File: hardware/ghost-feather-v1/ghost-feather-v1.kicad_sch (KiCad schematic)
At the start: 71 parts, among them J1 Conn_ARM_SWD_TagConnect_TC2030, J2 USB_C_Receptacle_USB2.0, J3 Conn_01x03, J4 Conn_01x03, J5 Conn_01x03, J6 Conn_01x03, J7 Conn_01x08, Q1 BSS138, Q2 BSS138, Q3 BSS138, Q4 BSS138, SW2 BOOT0, U1 STM32F722RETx, U2 BMI270, U3 USBLC6-2SC6_MOD, U4 MPM3610, U5 MPM3610, X1 16MHz, X2 32kHz768

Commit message: feat: Add crystal and clock oscillator footprints #1
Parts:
- C1: footprint Capacitor_SMD:C_0603_1608Metric -> ghost-feather-v1:CC4V-T1A-32.768kHz
- X1: footprint (none) -> ghost-feather-v1:AMPMGFB_1.6mm1.2mm_16MHz
- X2: footprint (none) -> ghost-feather-v1:CC4V-T1A-32.768kHz
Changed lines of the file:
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@@
       (effects (font (size 1.27 1.27)))
     )
-    (property "Footprint" "" (at 328.93 116.84 0)
+    (property "Footprint" "ghost-feather-v1:AMPMGFB_1.6mm1.2mm_16MHz" (at 328.93 116.84 0)
       (effects (font (size 1.27 1.27)) hide)
     )
@@
       (effects (font (size 1.27 1.27)) (justify right))
     )
-    (property "Footprint" "" (at 317.5 165.1 0)
+    (property "Footprint" "ghost-feather-v1:CC4V-T1A-32.768kHz" (at 317.5 165.1 0)
       (effects (font (size 1.27 1.27)) hide)
     )
@@
       (effects (font (size 1.27 1.27)) (justify right))
     )
-    (property "Footprint" "Capacitor_SMD:C_0603_1608Metric" (at 247.65 92.71 0)
-      (effects (font (size 1.27 1.27)) hide)
-    )
+    (property "Footprint" "ghost-feather-v1:CC4V-T1A-32.768kHz" (at 247.65 92.71 0)
+      (effects (font (size 1.27 1.27)) hide)
+    )

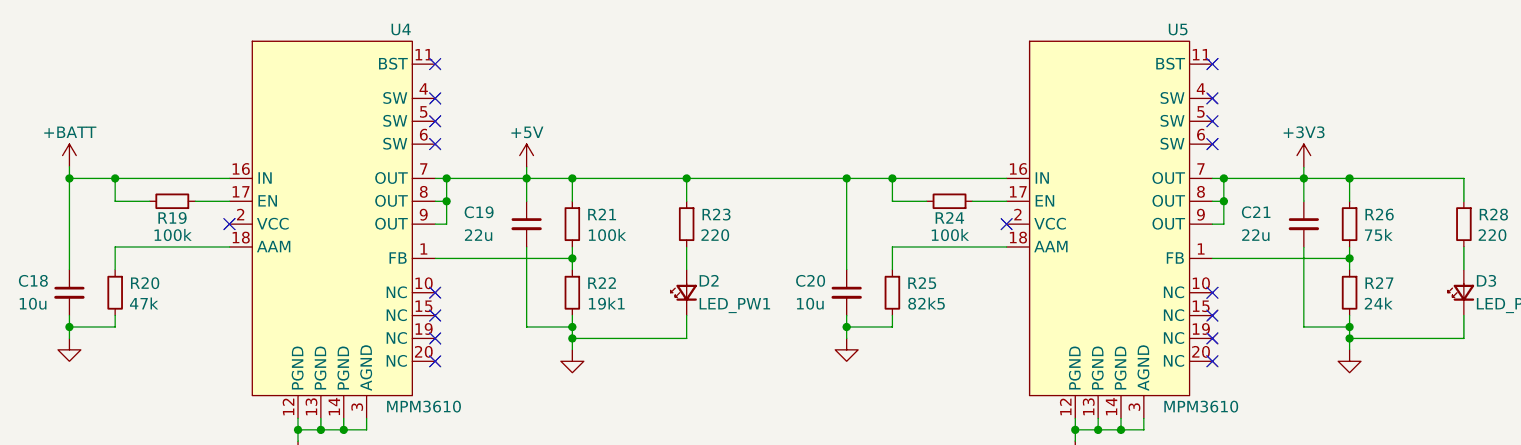
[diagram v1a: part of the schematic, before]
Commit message: feat: Add power flags to pass ERC
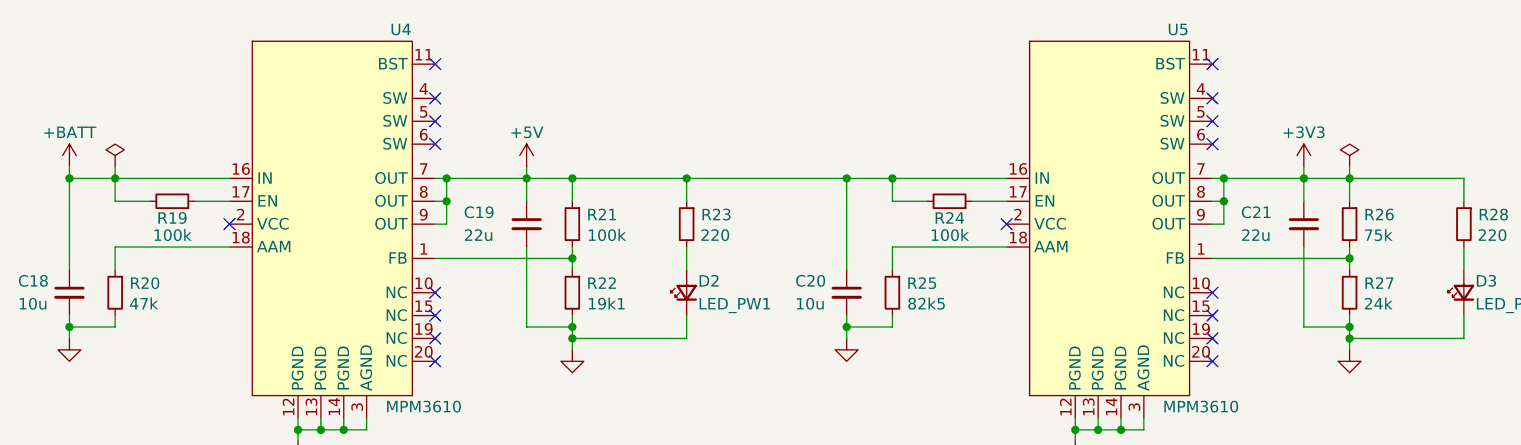
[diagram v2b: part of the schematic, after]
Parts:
- C1: footprint ghost-feather-v1:CC4V-T1A-32.768kHz -> Capacitor_SMD:C_0402_1005Metric
- SW2: footprint Connector_USB:USB_C_Receptacle_GCT_USB4085 -> Button_Switch_SMD:SW_SPST_EVQPE1
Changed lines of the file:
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@@
     (stroke (width 0) (type default))
   )
+  (wire (pts (xy 80.01 46.99) (xy 80.01 48.26))
+    (stroke (width 0) (type default))
+  )
   (wire (pts (xy 167.64 189.23) (xy 168.91 189.23))
     (stroke (width 0) (type default))
@@
     (stroke (width 0) (type default))
   )
+  (wire (pts (xy 217.17 46.99) (xy 217.17 48.26))
+    (stroke (width 0) (type default))
+  )
   (wire (pts (xy 116.84 53.34) (xy 116.84 50.8))
     (stroke (width 0) (type default))
@@
     )
   )
+  (symbol (lib_id "power:PWR_FLAG") (at 217.17 46.99 0) (unit 1)
+    (in_bom yes) (on_board yes) (dnp no) (fields_autoplaced)
+    (property "Reference" "#FLG04" (at 217.17 45.085 0)
+      (effects (font (size 1.27 1.27)) hide)
+    )
+    (property "Value" "PWR_FLAG" (at 217.17 41.91 0)
+      (effects (font (size 1.27 1.27)) hide)
+    )
+    (property "Footprint" "" (at 217.17 46.99 0)
+      (effects (font (size 1.27 1.27)) hide)
+    )
+    (property "Datasheet" "~" (at 217.17 46.99 0)
+      (effects (font (size 1.27 1.27)) hide)
+    )
+    (pin "1")
+    (instances
+      (project "ghost-feather-v1"
+        (path "/e4b634d1-7d64-4f26-a94e-3707be1de22a"
+          (reference "#FLG04") (unit 1)
+        )
+      )
+    )
+  )
   (symbol (lib_id "Device:C_Small") (at 298.45 92.71 0) (mirror y) (unit 1)
     (in_bom yes) (on_board yes) (dnp no) (fields_autoplaced)
@@
     )
   )
+  (symbol (lib_id "power:PWR_FLAG") (at 80.01 46.99 0) (unit 1)
+    (in_bom yes) (on_board yes) (dnp no) (fields_autoplaced)
+    (property "Reference" "#FLG03" (at 80.01 45.085 0)
+      (effects (font (size 1.27 1.27)) hide)
+    )
+    (property "Value" "PWR_FLAG" (at 80.01 41.91 0)
+      (effects (font (size 1.27 1.27)) hide)
+    )
+    (property "Footprint" "" (at 80.01 46.99 0)
+      (effects (font (size 1.27 1.27)) hide)
+    )
+    (property "Datasheet" "~" (at 80.01 46.99 0)
+      (effects (font (size 1.27 1.27)) hide)
+    )
+    (pin "1")
+    (instances
+      (project "ghost-feather-v1"
+        (path "/e4b634d1-7d64-4f26-a94e-3707be1de22a"
+          (reference "#FLG03") (unit 1)
+        )
+      )
+    )
+  )
   (symbol (lib_id "power:GND") (at 308.61 107.95 0) (mirror y) (unit 1)
     (in_bom yes) (on_board yes) (dnp no) (fields_autoplaced)
@@
       (effects (font (size 1.27 1.27)))
     )
-    (property "Footprint" "Connector_USB:USB_C_Receptacle_GCT_USB4085" (at 344.17 130.81 0)
+    (property "Footprint" "Button_Switch_SMD:SW_SPST_EVQPE1" (at 344.17 130.81 0)
       (effects (font (size 1.27 1.27)) hide)
     )
@@
       (effects (font (size 1.27 1.27)) (justify right))
     )
-    (property "Footprint" "ghost-feather-v1:CC4V-T1A-32.768kHz" (at 247.65 92.71 0)
+    (property "Footprint" "Capacitor_SMD:C_0402_1005Metric" (at 247.65 92.71 0)
       (effects (font (size 1.27 1.27)) hide)
     )

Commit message: feat: Components placement on PCB #2
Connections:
- net RF_CH0: now also U1.35 (PB14); no longer U1.37 (PC6)
- net RF_CH1: now also U1.36 (PB15); no longer U1.38 (PC7)
- net RF_CH2: now also U1.37 (PC6); no longer U1.39 (PC8)
- net RF_CH3: now also U1.38 (PC7); no longer U1.40 (PC9)
- net RF_CH4: now also U1.39 (PC8); no longer U1.36 (PB15)
- net RF_CH5: now also U1.40 (PC9); no longer U1.35 (PB14)
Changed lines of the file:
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@@
+    (stroke (width 0) (type default))
+  )
+  (wire (pts (xy 353.06 153.67) (xy 335.28 153.67))
     (stroke (width 0) (type default))
   )
@@
     (stroke (width 0) (type default))
   )
-  (wire (pts (xy 290.83 146.05) (xy 353.06 146.05))
-    (stroke (width 0) (type default))
-  )
   (wire (pts (xy 189.23 76.2) (xy 189.23 74.93))
     (stroke (width 0) (type default))
@@
     (stroke (width 0) (type default))
   )
+  (wire (pts (xy 347.98 143.51) (xy 347.98 207.01))
+    (stroke (width 0) (type default))
+  )
   (wire (pts (xy 237.49 148.59) (xy 227.33 148.59))
     (stroke (width 0) (type default))
@@
     (stroke (width 0) (type default))
   )
-  (wire (pts (xy 290.83 151.13) (xy 353.06 151.13))
-    (stroke (width 0) (type default))
-  )
   (wire (pts (xy 303.53 168.91) (xy 303.53 166.37))
     (stroke (width 0) (type default))
@@
     (stroke (width 0) (type default))
   )
+  (wire (pts (xy 353.06 148.59) (xy 340.36 148.59))
+    (stroke (width 0) (type default))
+  )
   (wire (pts (xy 217.17 219.71) (xy 217.17 217.17))
     (stroke (width 0) (type default))
@@
     (stroke (width 0) (type default))
   )
+  (wire (pts (xy 345.44 146.05) (xy 353.06 146.05))
+    (stroke (width 0) (type default))
+  )
   (wire (pts (xy 336.55 130.81) (xy 339.09 130.81))
     (stroke (width 0) (type default))
@@
     (stroke (width 0) (type default))
   )
+  (wire (pts (xy 340.36 148.59) (xy 340.36 143.51))
+    (stroke (width 0) (type default))
+  )
   (wire (pts (xy 208.28 247.65) (xy 217.17 247.65))
     (stroke (width 0) (type default))
@@
     (stroke (width 0) (type default))
   )
-  (wire (pts (xy 243.84 207.01) (xy 345.44 207.01))
+  (wire (pts (xy 243.84 207.01) (xy 347.98 207.01))
     (stroke (width 0) (type default))
   )
@@
     (stroke (width 0) (type default))
   )
+  (wire (pts (xy 332.74 156.21) (xy 353.06 156.21))
+    (stroke (width 0) (type default))
+  )
   (wire (pts (xy 167.64 224.79) (xy 168.91 224.79))
     (stroke (width 0) (type default))
@@
     (stroke (width 0) (type default))
   )
+  (wire (pts (xy 290.83 143.51) (xy 340.36 143.51))
+    (stroke (width 0) (type default))
+  )
   (wire (pts (xy 138.43 86.36) (xy 138.43 106.68))
     (stroke (width 0) (type default))
@@
     (stroke (width 0) (type default))
   )
-  (wire (pts (xy 246.38 204.47) (xy 342.9 204.47))
+  (wire (pts (xy 246.38 204.47) (xy 345.44 204.47))
     (stroke (width 0) (type default))
   )
@@
     (stroke (width 0) (type default))
   )
-  (wire (pts (xy 345.44 207.01) (xy 345.44 156.21))
-    (stroke (width 0) (type default))
-  )
-  (wire (pts (xy 345.44 156.21) (xy 353.06 156.21))
-    (stroke (width 0) (type default))
-  )
   (wire (pts (xy 328.93 124.46) (xy 328.93 125.73))
     (stroke (width 0) (type default))
@@
     (stroke (width 0) (type default))
   )
+  (wire (pts (xy 290.83 151.13) (xy 332.74 151.13))
+    (stroke (width 0) (type default))
+  )
   (wire (pts (xy 186.69 101.6) (xy 204.47 101.6))
     (stroke (width 0) (type default))
@@
     (stroke (width 0) (type default))
   )
-  (wire (pts (xy 290.83 143.51) (xy 353.06 143.51))
-    (stroke (width 0) (type default))
-  )
   (wire (pts (xy 173.99 209.55) (xy 168.91 209.55))
     (stroke (width 0) (type default))
@@
     (stroke (width 0) (type default))
   )
+  (wire (pts (xy 337.82 151.13) (xy 337.82 146.05))
+    (stroke (width 0) (type default))
+  )
   (wire (pts (xy 116.84 48.26) (xy 116.84 50.8))
     (stroke (width 0) (type default))
@@
     (stroke (width 0) (type default))
   )
+  (wire (pts (xy 353.06 151.13) (xy 337.82 151.13))
+    (stroke (width 0) (type default))
+  )
   (wire (pts (xy 102.87 76.2) (xy 105.41 76.2))
     (stroke (width 0) (type default))
   )
+  (wire (pts (xy 345.44 146.05) (xy 345.44 204.47))
+    (stroke (width 0) (type default))
+  )
   (wire (pts (xy 353.06 140.97) (xy 351.79 140.97))
     (stroke (width 0) (type default))
@@
     (stroke (width 0) (type default))
   )
+  (wire (pts (xy 335.28 153.67) (xy 335.28 148.59))
+    (stroke (width 0) (type default))
+  )
   (wire (pts (xy 265.43 88.9) (xy 265.43 102.87))
     (stroke (width 0) (type default))
@@
     (stroke (width 0) (type default))
   )
-  (wire (pts (xy 342.9 204.47) (xy 342.9 153.67))
-    (stroke (width 0) (type default))
-  )
   (wire (pts (xy 308.61 96.52) (xy 298.45 96.52))
     (stroke (width 0) (type default))
@@
     (stroke (width 0) (type default))
   )
-  (wire (pts (xy 290.83 148.59) (xy 353.06 148.59))
-    (stroke (width 0) (type default))
-  )
   (wire (pts (xy 243.84 134.62) (xy 243.84 138.43))
     (stroke (width 0) (type default))
@@
     (stroke (width 0) (type default))
   )
+  (wire (pts (xy 335.28 148.59) (xy 290.83 148.59))
+    (stroke (width 0) (type default))
+  )
   (wire (pts (xy 217.17 195.58) (xy 217.17 196.85))
     (stroke (width 0) (type default))
@@
     (stroke (width 0) (type default))
   )
+  (wire (pts (xy 337.82 146.05) (xy 290.83 146.05))
+    (stroke (width 0) (type default))
+  )
   (wire (pts (xy 217.17 66.04) (xy 217.17 67.31))
     (stroke (width 0) (type default))
@@
     (stroke (width 0) (type default))
   )
+  (wire (pts (xy 332.74 151.13) (xy 332.74 156.21))
+    (stroke (width 0) (type default))
+  )
   (wire (pts (xy 161.29 64.77) (xy 166.37 64.77))
     (stroke (width 0) (type default))
@@
     (stroke (width 0) (type default))
   )
+  (wire (pts (xy 347.98 143.51) (xy 353.06 143.51))
+    (stroke (width 0) (type default))
+  )
   (wire (pts (xy 327.66 161.29) (xy 332.74 161.29))
-    (stroke (width 0) (type default))
-  )
-  (wire (pts (xy 342.9 153.67) (xy 353.06 153.67))
     (stroke (width 0) (type default))
   )
@@
     (effects (font (size 1.27 1.27) (thickness 0.254) bold) (justify left bottom))
   )
-  (label "RF_CH1" (at 291.465 146.05 0) (fields_autoplaced)
+  (label "RF_CH3" (at 291.465 146.05 0) (fields_autoplaced)
     (effects (font (size 1.27 1.27) (thickness 0.254) bold) (justify left bottom))
   )
@@
     (effects (font (size 1.27 1.27) (thickness 0.254) bold) (justify right bottom))
   )
-  (label "RF_CH5" (at 254.635 186.69 180) (fields_autoplaced)
+  (label "RF_CH0" (at 254.635 186.69 180) (fields_autoplaced)
     (effects (font (size 1.27 1.27) (thickness 0.254) bold) (justify right bottom))
   )
@@
     (effects (font (size 1.27 1.27) (thickness 0.254) bold) (justify right bottom))
   )
-  (label "RF_CH3" (at 291.465 151.13 0) (fields_autoplaced)
+  (label "RF_CH5" (at 291.465 151.13 0) (fields_autoplaced)
     (effects (font (size 1.27 1.27) (thickness 0.254) bold) (justify left bottom))
   )
@@
     (effects (font (size 1.27 1.27) (thickness 0.254) bold) (justify right bottom))
   )
-  (label "RF_CH4" (at 254.635 189.23 180) (fields_autoplaced)
+  (label "RF_CH1" (at 254.635 189.23 180) (fields_autoplaced)
     (effects (font (size 1.27 1.27) (thickness 0.254) bold) (justify right bottom))
   )
@@
     (effects (font (size 1.27 1.27) (thickness 0.254) bold) (justify right bottom))
   )
-  (label "RF_CH2" (at 291.465 148.59 0) (fields_autoplaced)
+  (label "RF_CH4" (at 291.465 148.59 0) (fields_autoplaced)
     (effects (font (size 1.27 1.27) (thickness 0.254) bold) (justify left bottom))
   )
@@
     (effects (font (size 1.27 1.27) (thickness 0.254) bold) (justify right bottom))
   )
-  (label "RF_CH0" (at 291.465 143.51 0) (fields_autoplaced)
+  (label "RF_CH2" (at 291.465 143.51 0) (fields_autoplaced)
     (effects (font (size 1.27 1.27) (thickness 0.254) bold) (justify left bottom))
   )
@@
     (pin "4")
     (pin "5")
+    (pin "8")
+    (pin "9")
     (pin "6")
     (pin "7")
-    (pin "8")
-    (pin "9")
-    (instances
-      (project "ghost-feather-v1"
+    (instances
+      (project "ghost-feather-v1"

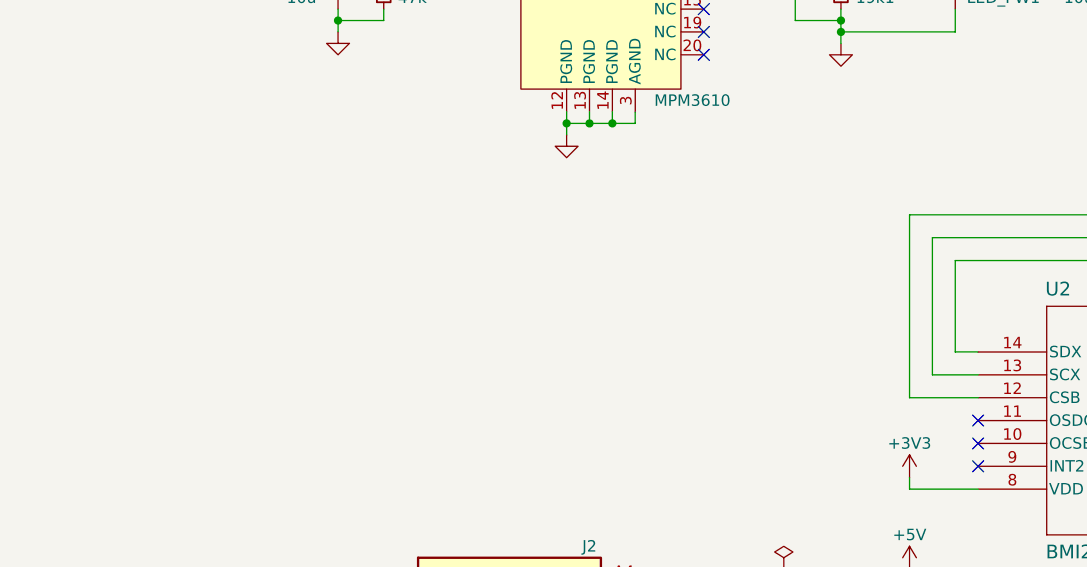
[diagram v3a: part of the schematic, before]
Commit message: feat: Components placement on PCB #3
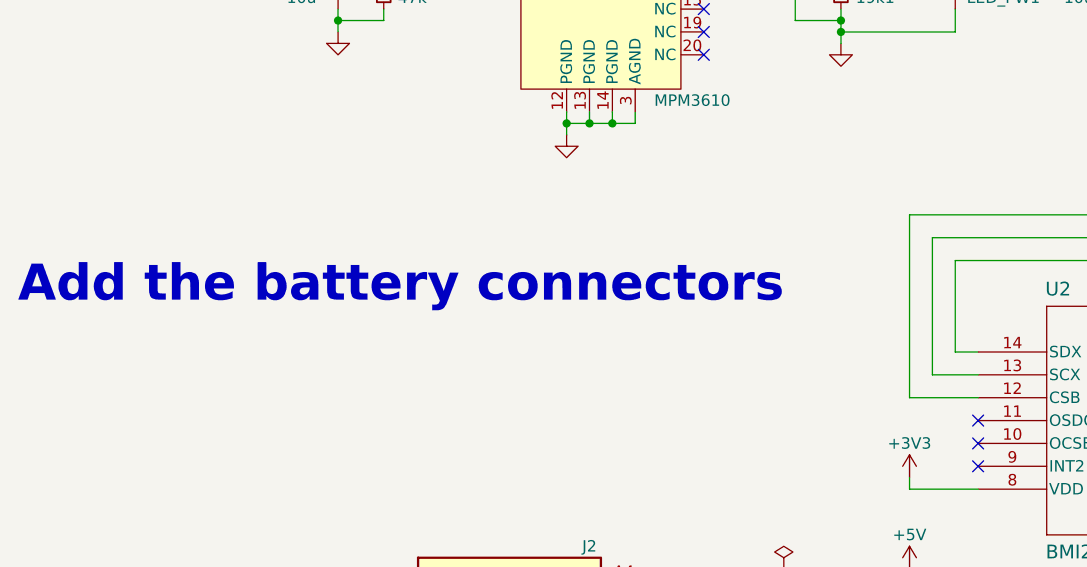
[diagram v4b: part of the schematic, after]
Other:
- note added: "Add the battery connectors"
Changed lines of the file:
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@@
     (stroke (width 0) (type default))
+  )
+  (text "Add the battery connectors" (at 39.37 96.52 0)
+    (effects (font (size 4 4) (thickness 0.8) bold) (justify left bottom))
   )
   (text "ESC PROBRABLY WILL HAVE THE 5V LOGIC LEVEL\nUSE THE SINGLE MOSFET LOGIC LEVEL SHIFTER\nFOR EACH ESCs\n"

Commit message: feat: PCB routing #1
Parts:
- J2: footprint Connector_USB:USB_C_Receptacle_GCT_USB4085 -> Connector_USB:USB_C_Receptacle_GCT_USB4105-xx-A_16P_TopMnt_Horizontal
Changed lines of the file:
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@@
       (effects (font (size 1.27 1.27)) hide)
     )
-    (property "Footprint" "Connector_USB:USB_C_Receptacle_GCT_USB4085" (at 97.79 142.24 0)
+    (property "Footprint" "Connector_USB:USB_C_Receptacle_GCT_USB4105-xx-A_16P_TopMnt_Horizontal" (at 97.79 142.24 0)
       (effects (font (size 1.27 1.27)) hide)
     )

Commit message: feat: PCB routing #3
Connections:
- net USBC_DM renamed USBC_D-
- net USBC_DP renamed USBC_D+
- net USB_DM renamed USB_D-
- net USB_DP renamed USB_D+
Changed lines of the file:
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@@
     (effects (font (size 1.27 1.27) (thickness 0.254) bold) (justify right bottom))
   )
-  (label "USBC_DM" (at 127.635 140.97 180) (fields_autoplaced)
+  (label "USBC_D-" (at 127.635 140.97 180) (fields_autoplaced)
     (effects (font (size 1.27 1.27) (thickness 0.254) bold) (justify right bottom))
   )
@@
     (effects (font (size 1.27 1.27) (thickness 0.254) bold) (justify right bottom))
   )
-  (label "USB_DP" (at 254.635 138.43 180) (fields_autoplaced)
+  (label "USB_D+" (at 254.635 138.43 180) (fields_autoplaced)
     (effects (font (size 1.27 1.27) (thickness 0.254) bold) (justify right bottom))
   )
@@
     (effects (font (size 1.27 1.27) (thickness 0.254) bold) (justify right bottom))
   )
-  (label "USBC_DP" (at 127.635 146.05 180) (fields_autoplaced)
+  (label "USBC_D+" (at 127.635 146.05 180) (fields_autoplaced)
     (effects (font (size 1.27 1.27) (thickness 0.254) bold) (justify right bottom))
   )
@@
     (effects (font (size 1.27 1.27) (thickness 0.254) bold) (justify left bottom))
   )
-  (label "USB_DM" (at 254.635 135.89 180) (fields_autoplaced)
+  (label "USB_D-" (at 254.635 135.89 180) (fields_autoplaced)
     (effects (font (size 1.27 1.27) (thickness 0.254) bold) (justify right bottom))
   )

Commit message: feat: PCB routing #8. PCB cleanup #1
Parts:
- added FID1, FID2, FID3, FID4, FID5, FID6, FID7, FID8: Fiducial, Fiducial:Fiducial_1.5mm_Mask4.5mm, symbol Mechanical:Fiducial
- added H1, H10, H11, H12, H13, H14, H15, H16, H2, H3, H4, H5, H6, H7, H8, H9: MountingHole, MountingHole:MountingHole_2.7mm_M2.5, symbol Mechanical:MountingHole
- added J8: Conn_01x02, Connector_AMASS:AMASS_XT60PW-M_1x02_P7.20mm_Horizontal, symbol Connector_Generic:Conn_01x02
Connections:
- net +BATT: now also J8.2 (Pin_2)
- net GND: now also J8.1 (Pin_1)
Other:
- note removed: "Add the battery connectors"
